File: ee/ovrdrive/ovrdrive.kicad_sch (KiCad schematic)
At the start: 3 parts

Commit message: Working on the board.
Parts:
- added C1, C2, C3: 1uF, Capacitor_SMD:C_0603_1608Metric, symbol Device:C_Small
- added J1: USB_A, Connector_USB:USB_A_CNCTech_1001-011-01101_Horizontal, symbol Connector:USB_A
- added U?: 74AUC2G32, symbol 74xGxx:74AUC2G32
- U2: renamed from U?; value JDEC_FLASH -> FLASH
- gave numbers to parts that had none: 1
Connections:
- net at U1.10 (FD7): now also U2.44 (I/O7)
- net at U1.11 (FD6): now also U2.43 (I/O6)
- net at U1.12 (FD5): now also U2.42 (I/O5)
- net at U1.13 (FD4): now also U2.41 (I/O4)
- net at U1.18 (FD3): now also U2.32 (I/O3)
- net at U1.19 (FD2): now also U2.31 (I/O2)
- net at U1.20 (FD1): now also U2.30 (I/O1)
- net at U1.21 (FD0): now also U2.29 (I/O0)
- net ~{WP}: now reaches U1.23 (FNWP)
- net ~{WP}: now also U2.19 (~{WP})
- net ~{WE}: now reaches U1.24 (FNWP)
- net ~{WE}: now also U2.18 (~{WE})
- net ALE: now reaches U1.25 (FALE)
- net ALE: now also U2.17 (ALE)
- net CLE: now reaches U1.26 (FCLE)
- net CLE: now also U2.16 (CLE)
- net ~{RE}: now reaches U1.6 (FNRE)
- net ~{RE}: now also U2.8 (~{RE})
- net ~{CE}: now reaches U1.7 (FCE0)
- net ~{CE}: now also U?.1
- net at U2.9 (~{CE}): now also U?.7
- new net GND: U?.4 (GND)
- new net INHIBIT: U?.2
- new net VCC: U?.8 (VCC)
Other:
- note added: "Change the pin name on the part"
- moved on the sheet: U1, U2A, U2B

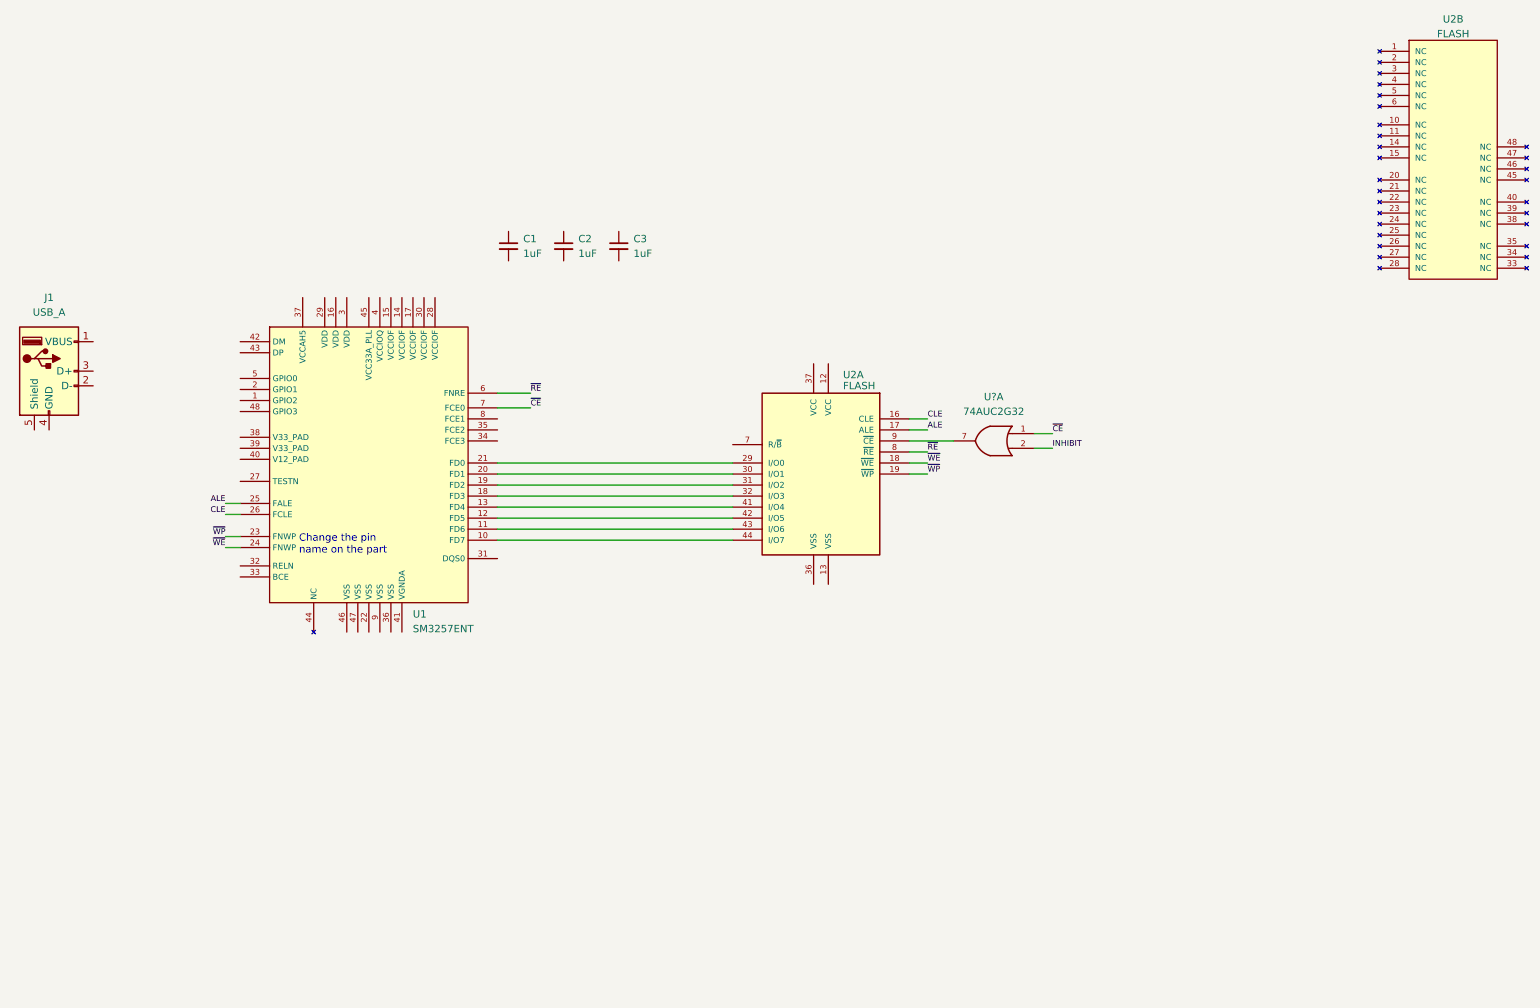
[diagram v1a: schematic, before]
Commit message: Updated the sm3257en to the correct pinout. Dropped some parts on the layout.
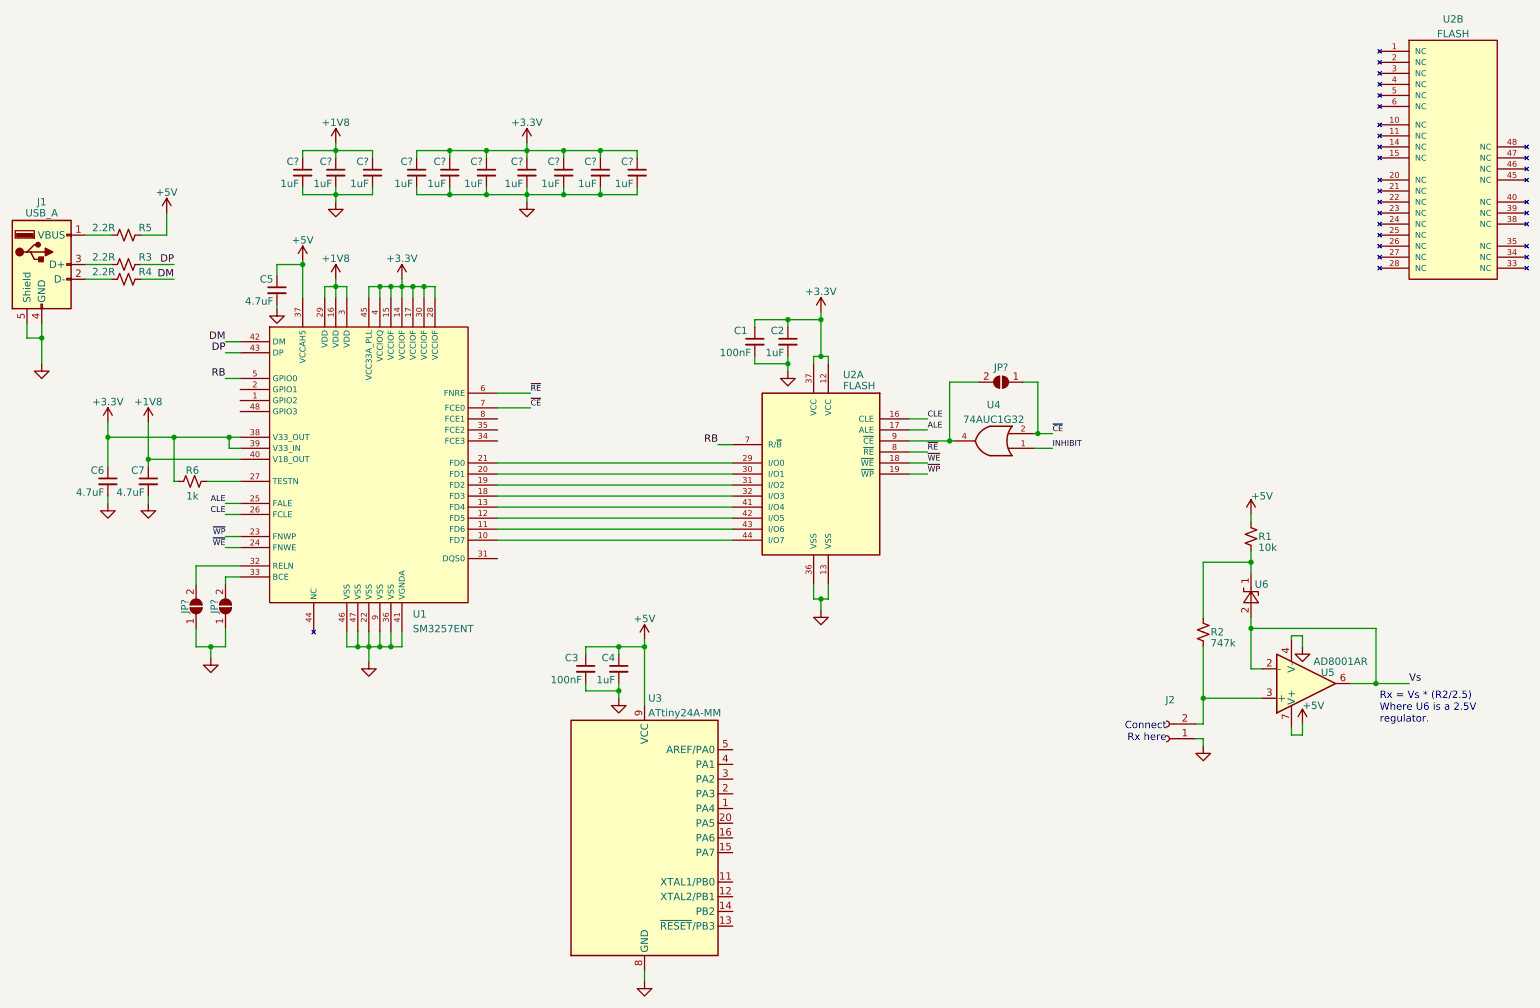
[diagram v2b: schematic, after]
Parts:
- removed C2: 1uF, Capacitor_SMD:C_0603_1608Metric, symbol Device:C_Small
- removed U?: 74AUC2G32, symbol 74xGxx:74AUC2G32
- added C3: 100nF, Capacitor_SMD:C_0603_1608Metric, symbol Device:C_Small
- added C4, C? (x10): 1uF, Capacitor_SMD:C_0603_1608Metric, symbol Device:C_Small
- added C5, C6, C7: 4.7uF, Capacitor_SMD:C_0603_1608Metric, symbol Device:C_Small
- added J2: Conn_01x02_Female, symbol Connector:Conn_01x02_Female
- added JP? (x3): SolderJumper_2_Open, symbol Jumper:SolderJumper_2_Open
- added R1: 10k, symbol Device:R_Small_US
- added R2: 747k, symbol Device:R_Small_US
- added R3, R4, R5: 2.2R, symbol Device:R_Small_US
- added R6: 1k, symbol Device:R_Small_US
- added U3: ATtiny24A-MM, Package_DFN_QFN:QFN-20-1EP_3x3mm_P0.45mm_EP1.6x1.6mm, symbol MCU_Microchip_ATtiny:ATtiny24A-MM
- added U4: 74AUC1G32, Package_TO_SOT_SMD:SOT-353_SC-70-5, symbol 74xGxx:74AUC1G32
- added U5: AD8001AR, Package_SO:SOIC-8_3.9x4.9mm_P1.27mm, symbol Amplifier_Operational:AD8001AR
- added U6: LM4040DBZ-2.5, Package_TO_SOT_SMD:SOT-23, symbol Reference_Voltage:LM4040DBZ-2.5
- C1: value 1uF -> 100nF
- U2: footprint TSOP48:tsop48 -> SOP50P2000X120-48N
- renumbered C3 to C2
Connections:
- net GND: now also C1.2, C2.2, J1.4 (GND), J1.5 (Shield), U1.22 (VSS), U1.36 (VSS), U1.41 (VGNDA), U1.46 (VSS), U1.47 (VSS), U1.9 (VSS), U2.13 (VSS), U2.36 (VSS), C3.2, C4.2, C5.2, C6.2, C7.2, C?.2, C?.2, C?.2, C?.2, C?.2, C?.2, C?.2, C?.2, C?.2, C?.2, J2.1 (Pin_1), JP?.1 (A), JP?.1 (A), U3.21 (GND), U3.8 (GND), U4.3 (GND), U5.4 (V-)
- net INHIBIT: now also U4.1
- net VCC: now also U4.5 (VCC)
- net ~{CE}: now also JP?.1 (A), U4.2
- net +3.3V: now reaches U1.14 (VCCIOF)
- net +3.3V: now also C1.1, C2.1, U1.15 (VCCIOF), U1.17 (VCCIOF), U1.28 (VCCIOF), U1.30 (VCCIOF), U1.38 (V33_OUT), U1.39 (V33_IN), U1.4 (VCCIOQ), U1.45 (VCC33A_PLL), U2.12 (VCC), U2.37 (VCC), C6.1, C?.1, C?.1, C?.1, C?.1, C?.1, C?.1, C?.1, R6.1
- net +1V8: now reaches U1.16 (VDD)
- net +1V8: now also U1.29 (VDD), U1.3 (VDD), U1.40 (V18_OUT), C7.1, C?.1, C?.1, C?.1
- net at U1.27 (TESTN): now also R6.2
- net at U1.32 (RELN): now also JP?.2 (B)
- net at U1.33 (BCE): now also JP?.2 (B)
- net +5V: now reaches U1.37 (VCCAH5)
- net +5V: now also C3.1, C4.1, C5.1, R1.1, R5.2, U3.9 (VCC), U5.7 (V+)
- net DM: now reaches U1.42 (DM)
- net DM: now also R4.2
- net DP: now reaches U1.43 (DP)
- net DP: now also R3.2
- net RB: now reaches U1.5 (GPIO0)
- net RB: now also U2.7 (R/~{B})
- net at J1.1 (VBUS): now also R5.1
- net at J1.2 (D-): now also R4.1
- net at J1.3 (D+): now also R3.1
- net at U2.9 (~{CE}): now also JP?.2 (B), U4.4
- new net: J2.2 (Pin_2), R2.2, U5.3 (+)
- new net: R1.2, R2.1, U6.1 (K)
- new net Vs: U5.2 (-), U5.6, U6.2 (A)
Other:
- note added: "Connect Rx here"
- note added: "Rx = Vs * (R2/2.5) Where U6 is a 2.5V regulator."
- note removed: "Change the pin name on the part"
- moved on the sheet: C2, J1

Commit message: Added design guides.
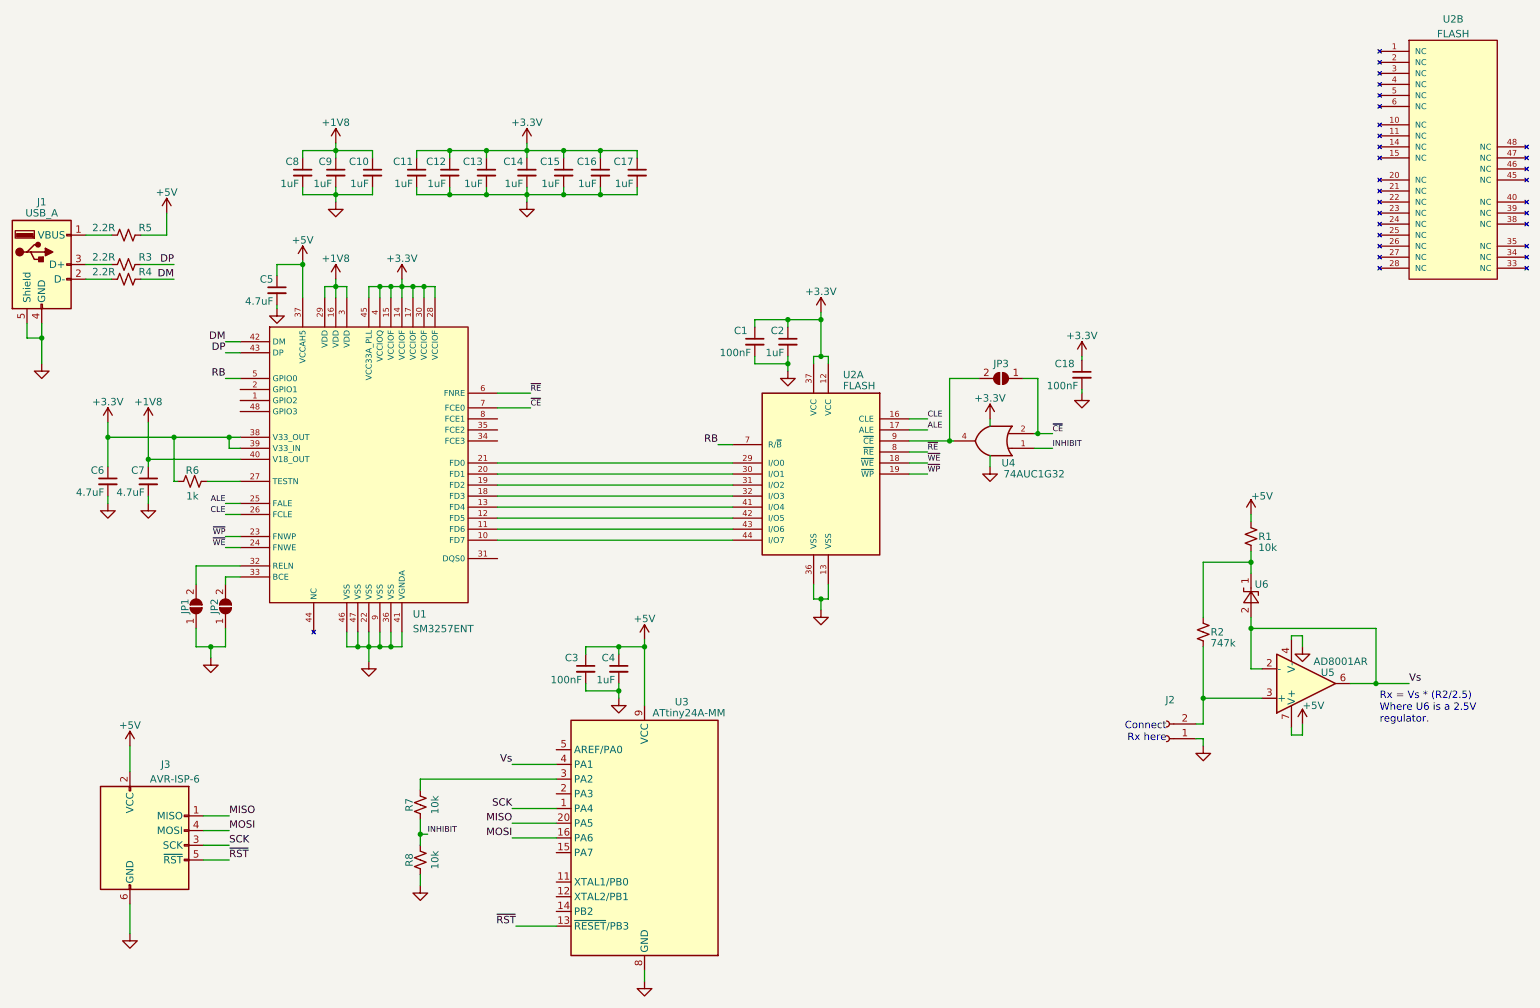
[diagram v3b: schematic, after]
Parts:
- added C18: 100nF, Capacitor_SMD:C_0603_1608Metric, symbol Device:C_Small
- added J3: AVR-ISP-6, Connector_PinHeader_2.54mm:PinHeader_2x03_P2.54mm_Vertical_SMD, symbol Connector:AVR-ISP-6
- added R7, R8: 10k, symbol Device:R_Small_US
- JP1, JP2, JP3: renamed from JP?; footprint (none) -> Jumper:SolderJumper-2_P1.3mm_Open_Pad1.0x1.5mm
- gave numbers to parts that had none: 10
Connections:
- net GND is gone; now on net +3.3V: C1.2, C10.2, C11.2, C12.2, C13.2, C14.2, C15.2, C16.2, C17.2, C2.2, C3.2, C4.2, C5.2, C6.2, C7.2, C8.2, C9.2, J1.4 (GND), J1.5 (Shield), J2.1 (Pin_1), JP1.1 (A), JP2.1 (A), U1.22 (VSS), U1.36 (VSS), U1.41 (VGNDA), U1.46 (VSS), U1.47 (VSS), U1.9 (VSS), U2.13 (VSS), U2.36 (VSS), U3.21 (GND), U3.8 (GND), U4.3 (GND), U5.4 (V-)
- net VCC is gone; now on net +3.3V: U4.5 (VCC)
- net +3.3V: now also C18.1, C18.2, J3.6 (GND), R8.1
- net +5V: now also J3.2 (VCC)
- net INHIBIT: now also R7.1, R8.2
- net Vs: now also U3.4 (PA1)
- net SCK: now reaches U3.1 (PA4)
- net SCK: now also J3.3 (SCK)
- net ~{RST}: now reaches U3.13 (~{RESET}/PB3)
- net ~{RST}: now also J3.5 (~{RST})
- net MOSI: now reaches U3.16 (PA6)
- net MOSI: now also J3.4 (MOSI)
- net MISO: now reaches U3.20 (PA5)
- net MISO: now also J3.1 (MISO)
- net at U3.3 (PA2): now also R7.2
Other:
- moved on the sheet: JP3, U3

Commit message: Added a bunch of mech parts.
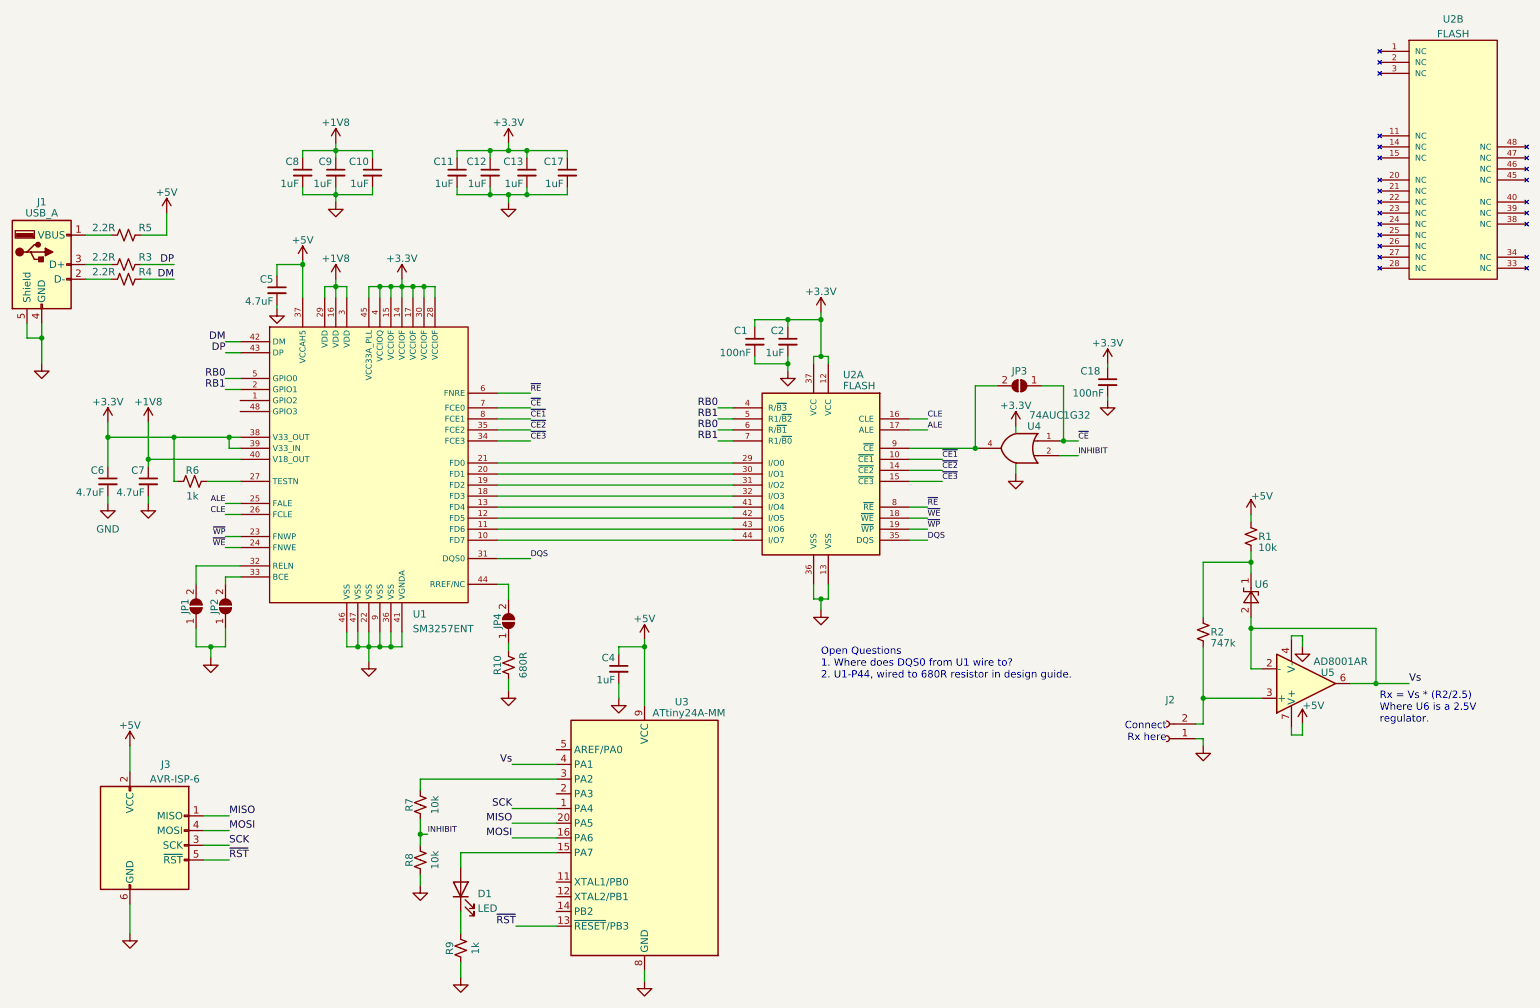
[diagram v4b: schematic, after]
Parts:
- removed C14, C15, C16: 1uF, Capacitor_SMD:C_0603_1608Metric, symbol Device:C_Small
- removed C3: 100nF, Capacitor_SMD:C_0603_1608Metric, symbol Device:C_Small
- added D1: LED, symbol Device:LED
- added JP4: SolderJumper_2_Open, Jumper:SolderJumper-2_P1.3mm_Open_Pad1.0x1.5mm, symbol Jumper:SolderJumper_2_Open
- added R10: 680R, Resistor_SMD:R_0603_1608Metric, symbol Device:R_Small_US
- added R9: 1k, Resistor_SMD:R_0603_1608Metric, symbol Device:R_Small_US
- R1, R2, R3, R4, R5, R6, R7, R8: footprint (none) -> Resistor_SMD:R_0603_1608Metric
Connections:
- net +3.3V: no longer C1.2, C10.2, C11.2, C12.2, C13.2, C17.2, C18.2, C2.2, C4.2, C5.2, C6.2, C7.2, C8.2, C9.2, J1.4 (GND), J1.5 (Shield), J2.1 (Pin_1), J3.6 (GND), JP1.1 (A), JP2.1 (A), R8.1, U1.22 (VSS), U1.36 (VSS), U1.41 (VGNDA), U1.46 (VSS), U1.47 (VSS), U1.9 (VSS), U2.13 (VSS), U2.36 (VSS), U3.21 (GND), U3.8 (GND), U4.3 (GND), U5.4 (V-)
- net INHIBIT: now also U4.2; no longer U4.1
- net ~{CE}: now also U4.1; no longer U4.2
- net RB1: now reaches U1.2 (GPIO1)
- net RB1: now also U2.5 (R1/~{B2}), U2.7 (R1/~{B0})
- net DQS: now reaches U1.31 (DQS0)
- net DQS: now also U2.35 (DQS)
- net ~{CE3}: now reaches U1.34 (FCE3)
- net ~{CE3}: now also U2.15 (~{CE3})
- net ~{CE2}: now reaches U1.35 (FCE2)
- net ~{CE2}: now also U2.14 (~{CE2})
- net at U1.44 (RREF/NC): now also JP4.2 (B)
- net ~{CE1}: now reaches U1.8 (FCE1)
- net ~{CE1}: now also U2.10 (~{CE1})
- net at U3.15 (PA7): now also D1.2 (A)
- net RB renamed RB0
- net RB0: now also U2.4 (R/~{B3}), U2.6 (R/~{B1}); no longer U2.7 (R/~{B})
- new net: JP4.1 (A), R10.2
- new net: D1.1 (K), R9.2
- new net GND: C1.2, C10.2, C11.2, C12.2, C13.2, C17.2, C18.2, C2.2, C4.2, C5.2, C6.2, C7.2, C8.2, C9.2, J1.4 (GND), J1.5 (Shield), J2.1 (Pin_1), J3.6 (GND), JP1.1 (A), JP2.1 (A), R10.1, R8.1, R9.1, U1.22 (VSS), U1.36 (VSS), U1.41 (VGNDA), U1.46 (VSS), U1.47 (VSS), U1.9 (VSS), U2.13 (VSS), U2.36 (VSS), U3.21 (GND), U3.8 (GND), U4.3 (GND), U5.4 (V-)
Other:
- note added: "Open Questions 1. Where does DQS0 from U1 wire to? 2. U1-P44, wired to 680R resistor in design guide."
- moved on the sheet: C11, C12, C13, C17, C18, JP3, U4

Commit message: Mech looking decent, new USB to fit in case.
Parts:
- J1: MPN (none) -> 0480372200
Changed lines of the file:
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@@
+      (effects (font (size 1.27 1.27)) hide)
+    )
+    (property "MPN" "0480372200" (id 4) (at 20.32 59.055 0)
       (effects (font (size 1.27 1.27)) hide)
     )

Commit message: Fit seems to be working.
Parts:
- removed JP3, JP4: SolderJumper_2_Open, Jumper:SolderJumper-2_P1.3mm_Open_Pad1.0x1.5mm, symbol Jumper:SolderJumper_2_Open
- removed U5: AD8001AR, Package_SO:SOIC-8_3.9x4.9mm_P1.27mm, symbol Amplifier_Operational:AD8001AR
- added C14, C3: 100nF, Capacitor_SMD:C_0603_1608Metric, symbol Device:C_Small
- added D2, D3: D, Diode_SMD:D_0603_1608Metric, symbol Device:D
- added Q1: Q_NMOS_DGS, Package_TO_SOT_SMD:SOT-23, symbol Device:Q_NMOS_DGS
- added R11: 2.2R, Resistor_SMD:R_0603_1608Metric, symbol Device:R_Small_US
- added U5: LMV321, Package_TO_SOT_SMD:SOT-23-5, symbol Amplifier_Operational:LMV321
- D1: footprint (none) -> LED_SMD:LED_0603_1608Metric
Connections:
- net +3.3V: now also Q1.3 (S)
- net +5V: now also D2.2 (A), U5.5 (V+)
- net GND: now also C14.2, R11.1, U5.2 (V-)
- net Vs: now also U5.3 (-), U5.4
- net at J2.2 (Pin_2), R2.2: now also U5.1 (+)
- net at R10.2: now also U1.44 (RREF/NC)
- net KILL: now reaches U3.2 (PA3)
- net KILL: now also Q1.2 (G), R11.2
- net Distruct_PWM: now reaches U3.5 (AREF/PA0)
- net Distruct_PWM: now also C3.2
- new net: C14.1, D3.1 (K), Q1.1 (D)
- new net: C3.1, D2.1 (K), D3.2 (A)
